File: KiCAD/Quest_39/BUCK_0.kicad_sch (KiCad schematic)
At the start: 21 parts

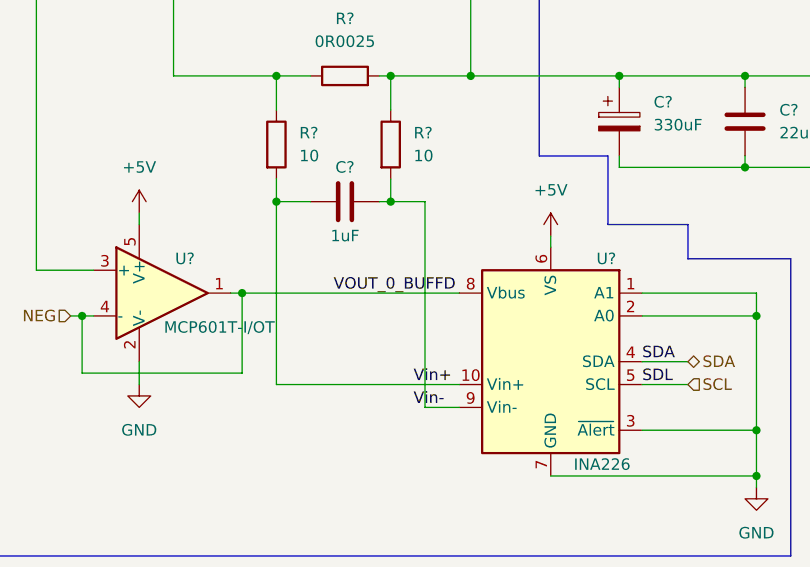
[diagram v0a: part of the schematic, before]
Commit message: Ordered BUCK_x schematic pages
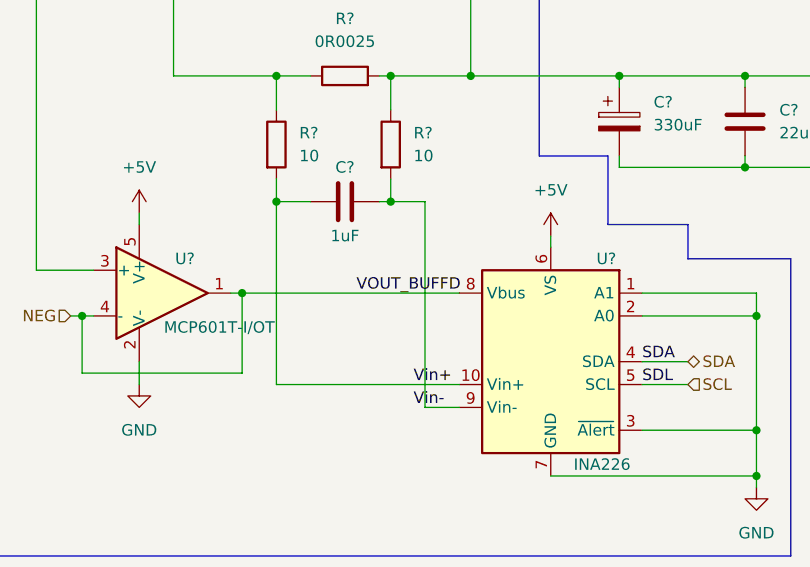
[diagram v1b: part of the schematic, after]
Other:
- title: Group_0 -> BUCK_0
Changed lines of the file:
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@@
   (paper "A3")
   (title_block
-    (title "Group_0")
-    (date "2022-11-28")
+    (title "BUCK_0")
+    (date "2022-12-05")
     (rev "0.1")
   )
@@
     (effects (font (size 1.27 1.27)) (justify left bottom))
   )
-  (label "VOUT_0_BUFFD" (at 55.88 74.93 0)
+  (label "VOUT_BUFFD" (at 58.42 74.93 0)
     (effects (font (size 1.27 1.27)) (justify left bottom))
   )

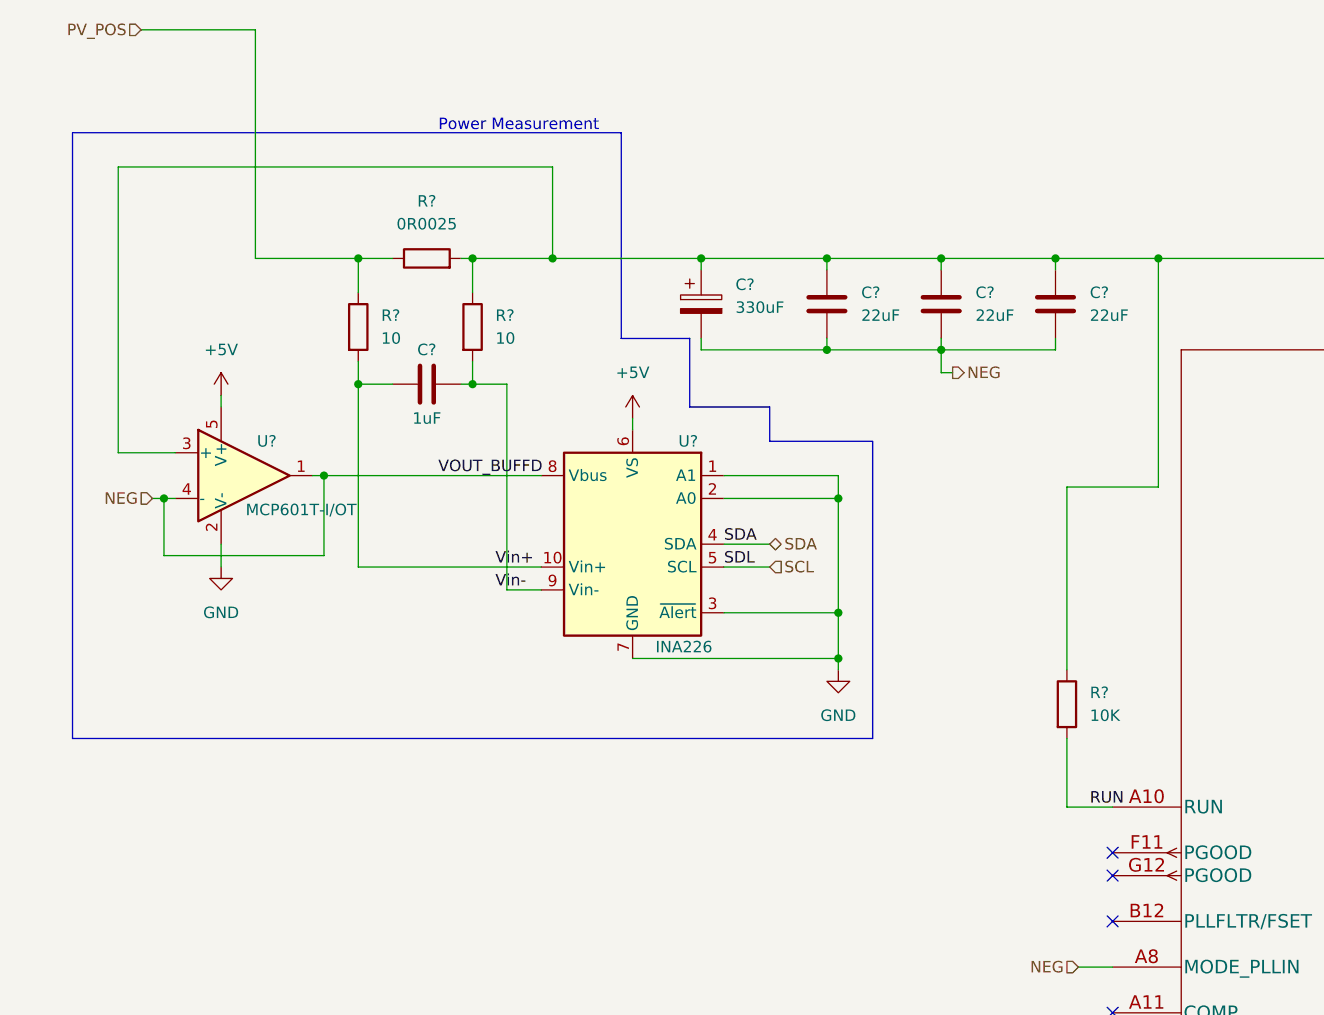
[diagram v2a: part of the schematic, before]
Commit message: Exchanged MCP601 for AD626
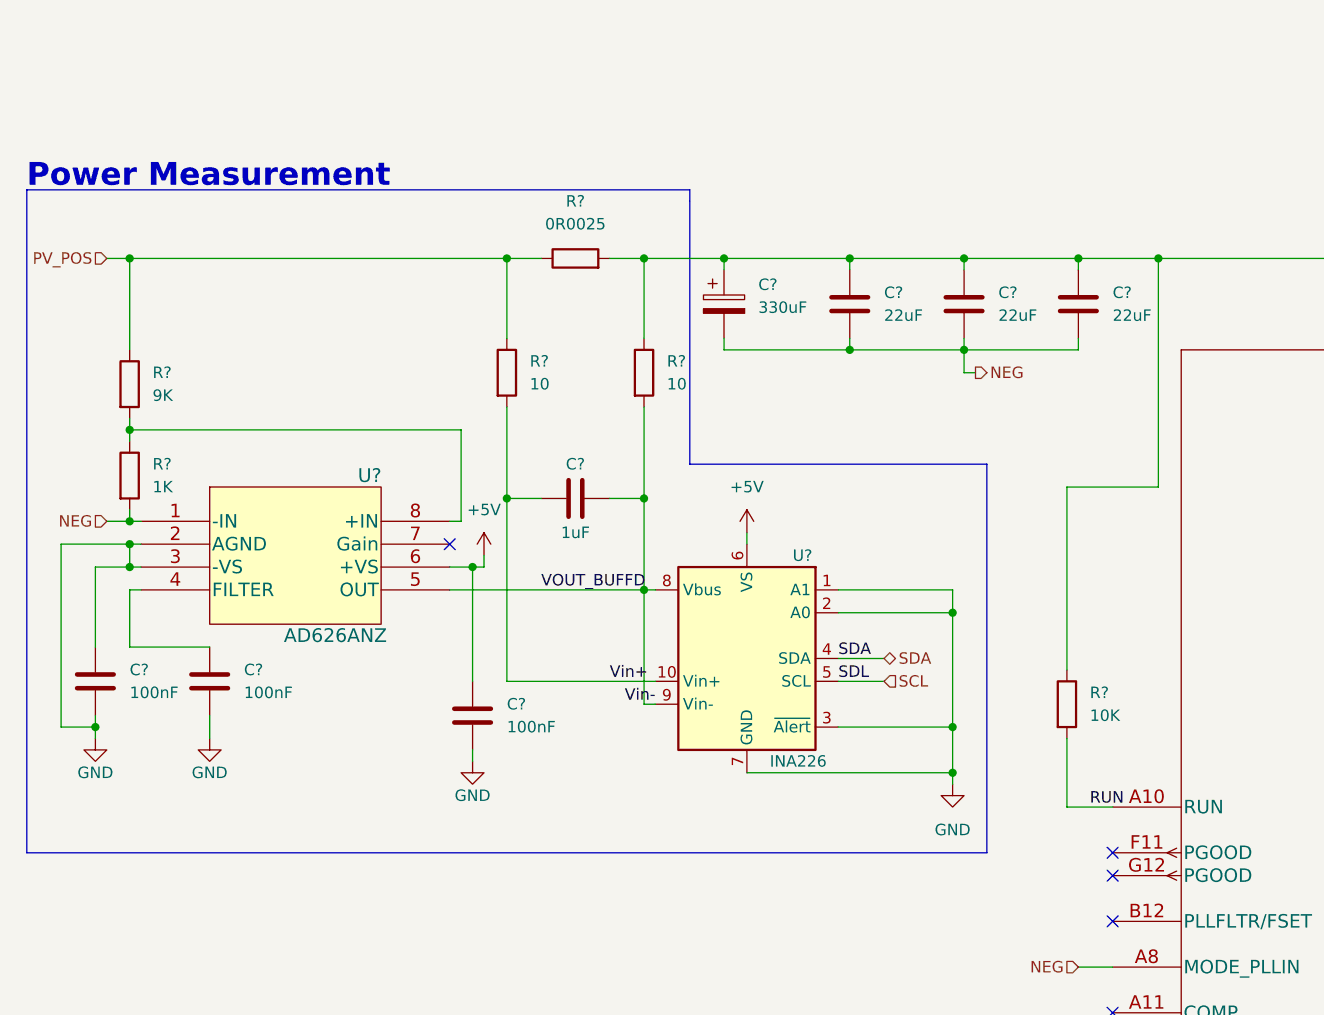
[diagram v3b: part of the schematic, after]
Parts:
- removed U?: MCP601T-I/OT, Package_TO_SOT_SMD:SOT-23-5, symbol Amplifier_Operational:MCP601-xOT
- added C? (x3): 100nF, symbol Device:C
- added R?: 9K, symbol Device:R
- added R?: 1K, symbol Device:R
- added U?: AD626ANZ, N_8_ADI, symbol AD626ANZ:AD626ANZ
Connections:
- net +5V: now also C?.1, U?.6 (+VS)
- net GND: now also C?.1, C?.2, C?.2, C?.2, U?.2 (AGND), U?.3 (-VS)
- net NEG: now also R?.2, U?.1 (-IN); no longer U?.8 (Vbus)
- net PV_POS: now also R?.1
- net VOUT_BUFFD: now reaches C?.2, R?.2, U?.9 (Vin-)
- net VOUT_BUFFD: now also U?.8 (Vbus), U?.5 (OUT)
- new net: C?.1, U?.4 (FILTER)
- new net: R?.1, R?.2, U?.8 (+IN)
- no-connect marks 16 -> 17
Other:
- moved on the sheet: C?, R?, U?

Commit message: Done TODO items
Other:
- moved on the sheet: C?
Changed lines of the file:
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@@
   (junction (at 321.31 162.56) (diameter 0) (color 0 0 0 0)
   )
+  (junction (at 382.27 185.42) (diameter 0) (color 0 0 0 0)
+  )
   (junction (at 201.93 215.9) (diameter 0) (color 0 0 0 0)
   )
@@
   )
   (junction (at 321.31 147.32) (diameter 0) (color 0 0 0 0)
-  )
-  (junction (at 382.27 185.42) (diameter 0) (color 0 0 0 0)
   )
   (junction (at 245.11 215.9) (diameter 0) (color 0 0 0 0)
@@
     (stroke (width 0) (type default) (color 0 0 0 0))
   )
+  (wire (pts (xy 382.27 182.88) (xy 382.27 185.42))
+    (stroke (width 0) (type default) (color 0 0 0 0))
+  )
   (wire (pts (xy 186.69 50.8) (xy 186.69 53.34))
     (stroke (width 0) (type default) (color 0 0 0 0))
@@
     (stroke (width 0) (type default) (color 0 0 0 0))
   )
+  (wire (pts (xy 369.57 182.88) (xy 369.57 185.42))
+    (stroke (width 0) (type default) (color 0 0 0 0))
+  )
+  (wire (pts (xy 355.6 182.88) (xy 355.6 185.42))
+    (stroke (width 0) (type default) (color 0 0 0 0))
+  )
   (wire (pts (xy 201.93 50.8) (xy 204.47 50.8))
     (stroke (width 0) (type default) (color 0 0 0 0))
   )
-  (wire (pts (xy 382.27 172.72) (xy 382.27 177.8))
+  (wire (pts (xy 382.27 172.72) (xy 382.27 175.26))
     (stroke (width 0) (type default) (color 0 0 0 0))
   )
@@
     (stroke (width 0) (type default) (color 0 0 0 0))
   )
-  (wire (pts (xy 369.57 172.72) (xy 369.57 177.8))
+  (wire (pts (xy 369.57 172.72) (xy 369.57 175.26))
     (stroke (width 0) (type default) (color 0 0 0 0))
   )
@@
     (stroke (width 0) (type default) (color 0 0 0 0))
   )
+  (wire (pts (xy 394.97 185.42) (xy 382.27 185.42))
+    (stroke (width 0) (type default) (color 0 0 0 0))
+  )
   (wire (pts (xy 81.28 50.8) (xy 81.28 59.69))
     (stroke (width 0) (type default) (color 0 0 0 0))
@@
     (stroke (width 0) (type default) (color 0 0 0 0))
   )
+  (wire (pts (xy 394.97 182.88) (xy 394.97 185.42))
+    (stroke (width 0) (type default) (color 0 0 0 0))
+  )
   (wire (pts (xy 90.17 60.96) (xy 104.14 60.96))
     (stroke (width 0) (type default) (color 0 0 0 0))
@@
     (stroke (width 0) (type default) (color 0 0 0 0))
   )
-  (wire (pts (xy 394.97 172.72) (xy 394.97 177.8))
+  (wire (pts (xy 394.97 172.72) (xy 394.97 175.26))
     (stroke (width 0) (type default) (color 0 0 0 0))
   )
@@
     (stroke (width 0) (type default) (color 0 0 0 0))
   )
-  (wire (pts (xy 355.6 172.72) (xy 355.6 177.8))
+  (wire (pts (xy 355.6 172.72) (xy 355.6 175.26))
     (stroke (width 0) (type default) (color 0 0 0 0))
   )
@@
   )
   (wire (pts (xy 115.57 87.63) (xy 115.57 90.17))
-    (stroke (width 0) (type default) (color 0 0 0 0))
-  )
-  (wire (pts (xy 382.27 185.42) (xy 394.97 185.42))
     (stroke (width 0) (type default) (color 0 0 0 0))
   )
@@
     (pin "2")
   )
-  (symbol (lib_id "Device:C_Polarized") (at 369.57 181.61 0) (unit 1)
+  (symbol (lib_id "Device:C_Polarized") (at 369.57 179.07 0) (unit 1)
     (in_bom yes) (on_board yes)
-    (property "Reference" "C?" (id 0) (at 373.3595 180.2975 0)
-      (effects (font (size 1.27 1.27)) (justify left))
-    )
-    (property "Value" "100uF" (id 1) (at 373.3595 182.8375 0)
-      (effects (font (size 1.27 1.27)) (justify left))
-    )
-    (property "Footprint" "" (id 2) (at 370.5352 185.42 0)
-      (effects (font (size 1.27 1.27)) hide)
-    )
-    (property "Datasheet" "~" (id 3) (at 369.57 181.61 0)
+    (property "Reference" "C?" (id 0) (at 373.3595 177.7575 0)
+      (effects (font (size 1.27 1.27)) (justify left))
+    )
+    (property "Value" "100uF" (id 1) (at 373.3595 180.2975 0)
+      (effects (font (size 1.27 1.27)) (justify left))
+    )
+    (property "Footprint" "" (id 2) (at 370.5352 182.88 0)
+      (effects (font (size 1.27 1.27)) hide)
+    )
+    (property "Datasheet" "~" (id 3) (at 369.57 179.07 0)
       (effects (font (size 1.27 1.27)) hide)
     )
@@
     (pin "2")
   )
-  (symbol (lib_id "Device:C_Polarized") (at 394.97 181.61 0) (unit 1)
+  (symbol (lib_id "Device:C_Polarized") (at 394.97 179.07 0) (unit 1)
     (in_bom yes) (on_board yes)
-    (property "Reference" "C?" (id 0) (at 398.7595 180.2975 0)
-      (effects (font (size 1.27 1.27)) (justify left))
-    )
-    (property "Value" "100uF" (id 1) (at 398.7595 182.8375 0)
-      (effects (font (size 1.27 1.27)) (justify left))
-    )
-    (property "Footprint" "" (id 2) (at 395.9352 185.42 0)
-      (effects (font (size 1.27 1.27)) hide)
-    )
-    (property "Datasheet" "~" (id 3) (at 394.97 181.61 0)
+    (property "Reference" "C?" (id 0) (at 398.7595 177.7575 0)
+      (effects (font (size 1.27 1.27)) (justify left))
+    )
+    (property "Value" "100uF" (id 1) (at 398.7595 180.2975 0)
+      (effects (font (size 1.27 1.27)) (justify left))
+    )
+    (property "Footprint" "" (id 2) (at 395.9352 182.88 0)
+      (effects (font (size 1.27 1.27)) hide)
+    )
+    (property "Datasheet" "~" (id 3) (at 394.97 179.07 0)
       (effects (font (size 1.27 1.27)) hide)
     )
@@
     (pin "8")
   )
-  (symbol (lib_id "Device:C_Polarized") (at 382.27 181.61 0) (unit 1)
+  (symbol (lib_id "Device:C_Polarized") (at 382.27 179.07 0) (unit 1)
     (in_bom yes) (on_board yes)
-    (property "Reference" "C?" (id 0) (at 386.0595 180.2975 0)
-      (effects (font (size 1.27 1.27)) (justify left))
-    )
-    (property "Value" "100uF" (id 1) (at 386.0595 182.8375 0)
-      (effects (font (size 1.27 1.27)) (justify left))
-    )
-    (property "Footprint" "" (id 2) (at 383.2352 185.42 0)
-      (effects (font (size 1.27 1.27)) hide)
-    )
-    (property "Datasheet" "~" (id 3) (at 382.27 181.61 0)
+    (property "Reference" "C?" (id 0) (at 386.0595 177.7575 0)
+      (effects (font (size 1.27 1.27)) (justify left))
+    )
+    (property "Value" "100uF" (id 1) (at 386.0595 180.2975 0)
+      (effects (font (size 1.27 1.27)) (justify left))
+    )
+    (property "Footprint" "" (id 2) (at 383.2352 182.88 0)
+      (effects (font (size 1.27 1.27)) hide)
+    )
+    (property "Datasheet" "~" (id 3) (at 382.27 179.07 0)
       (effects (font (size 1.27 1.27)) hide)
     )
@@
     (pin "1")
   )
-  (symbol (lib_id "Device:C_Polarized") (at 355.6 181.61 0) (unit 1)
+  (symbol (lib_id "Device:C_Polarized") (at 355.6 179.07 0) (unit 1)
     (in_bom yes) (on_board yes)
-    (property "Reference" "C?" (id 0) (at 359.3895 180.2975 0)
-      (effects (font (size 1.27 1.27)) (justify left))
-    )
-    (property "Value" "100uF" (id 1) (at 359.3895 182.8375 0)
-      (effects (font (size 1.27 1.27)) (justify left))
-    )
-    (property "Footprint" "" (id 2) (at 356.5652 185.42 0)
-      (effects (font (size 1.27 1.27)) hide)
-    )
-    (property "Datasheet" "~" (id 3) (at 355.6 181.61 0)
-      (effects (font (size 1.27 1.27)) hide)
-    )
+    (property "Reference" "C?" (id 0) (at 359.3895 177.7575 0)
+      (effects (font (size 1.27 1.27)) (justify left))
+    )
+    (property "Value" "100uF" (id 1) (at 359.3895 180.2975 0)
+      (effects (font (size 1.27 1.27)) (justify left))
+    )
+    (property "Footprint" "" (id 2) (at 356.5652 182.88 0)
+      (effects (font (size 1.27 1.27)) hide)
+    )
+    (property "Datasheet" "~" (id 3) (at 355.6 179.07 0)
+      (effects (font (size 1.27 1.27)) hide)
+    )

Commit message: Fixed most ERC errors
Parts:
- added TP6: TestPoint, symbol Connector:TestPoint
- gave numbers to parts that had none: 26
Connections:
- net GND: no longer U5.3 (~{Alert})
- net VOUT_BUFFD: now also TP6.1
- net Vfb: no longer C27.2, R12.1, U6.F12 (VFB)
- new net: C27.2, R12.1, U6.F12 (VFB)
- no-connect marks 17 -> 18
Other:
- moved on the sheet: C14, C15, C16, C17, C18, C19, C20, C21, C22, C23, C24, C25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

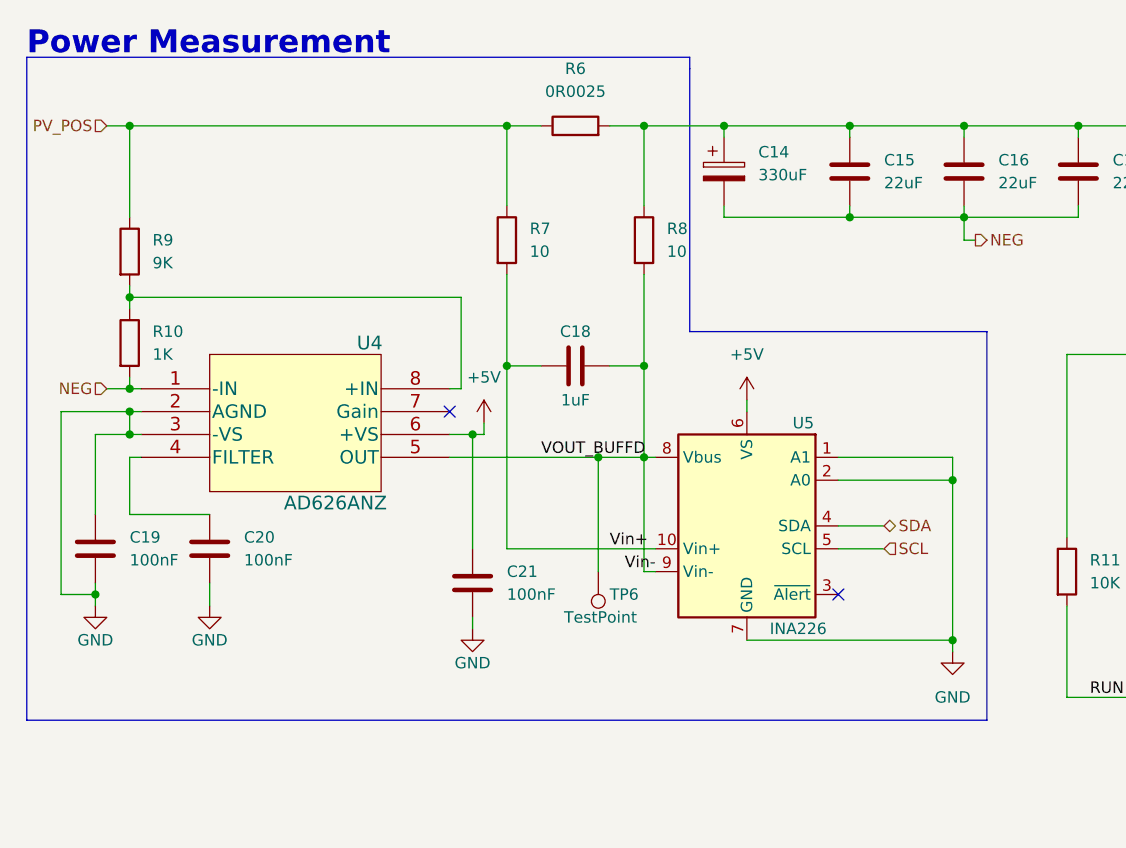
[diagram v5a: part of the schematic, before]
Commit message: Ordered and anotated components
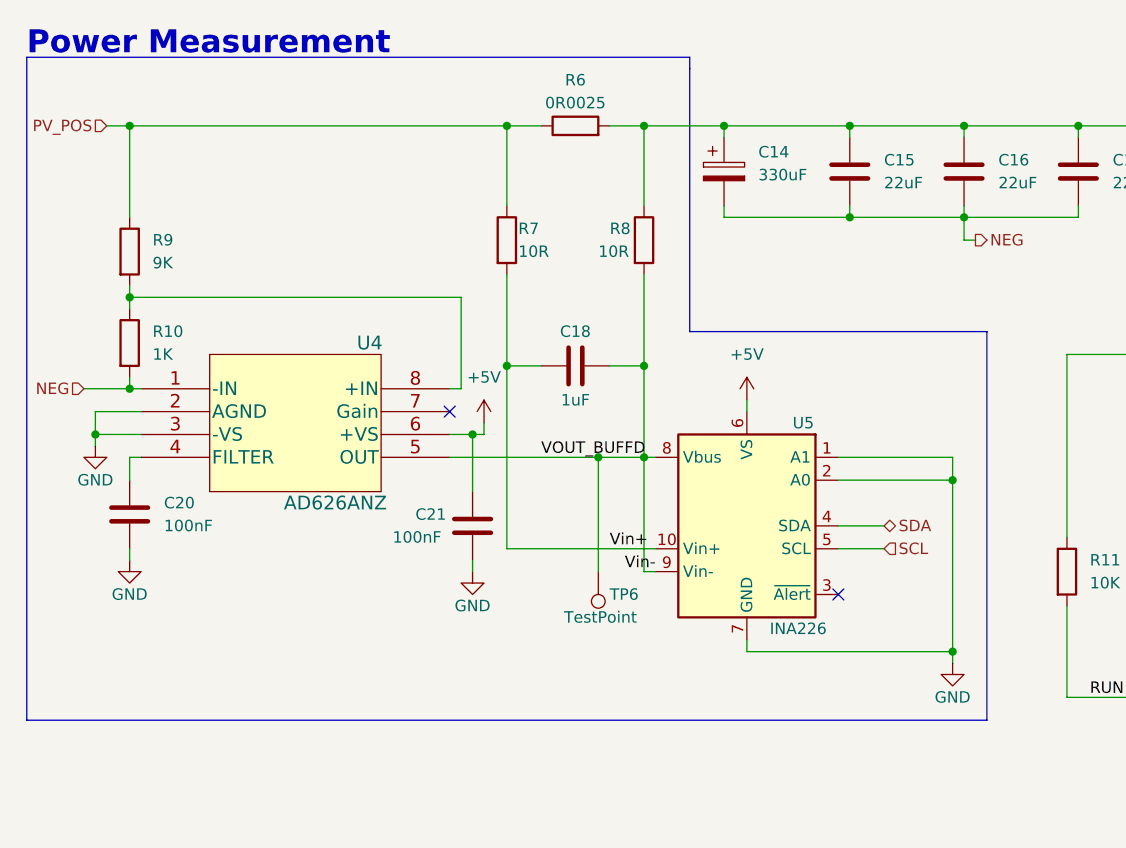
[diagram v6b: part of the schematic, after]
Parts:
- removed C19: 100nF, symbol Device:C
- R7, R8: value 10 -> 10R
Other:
- moved on the sheet: C20, C21
